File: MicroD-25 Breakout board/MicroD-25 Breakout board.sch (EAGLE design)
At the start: 1 part

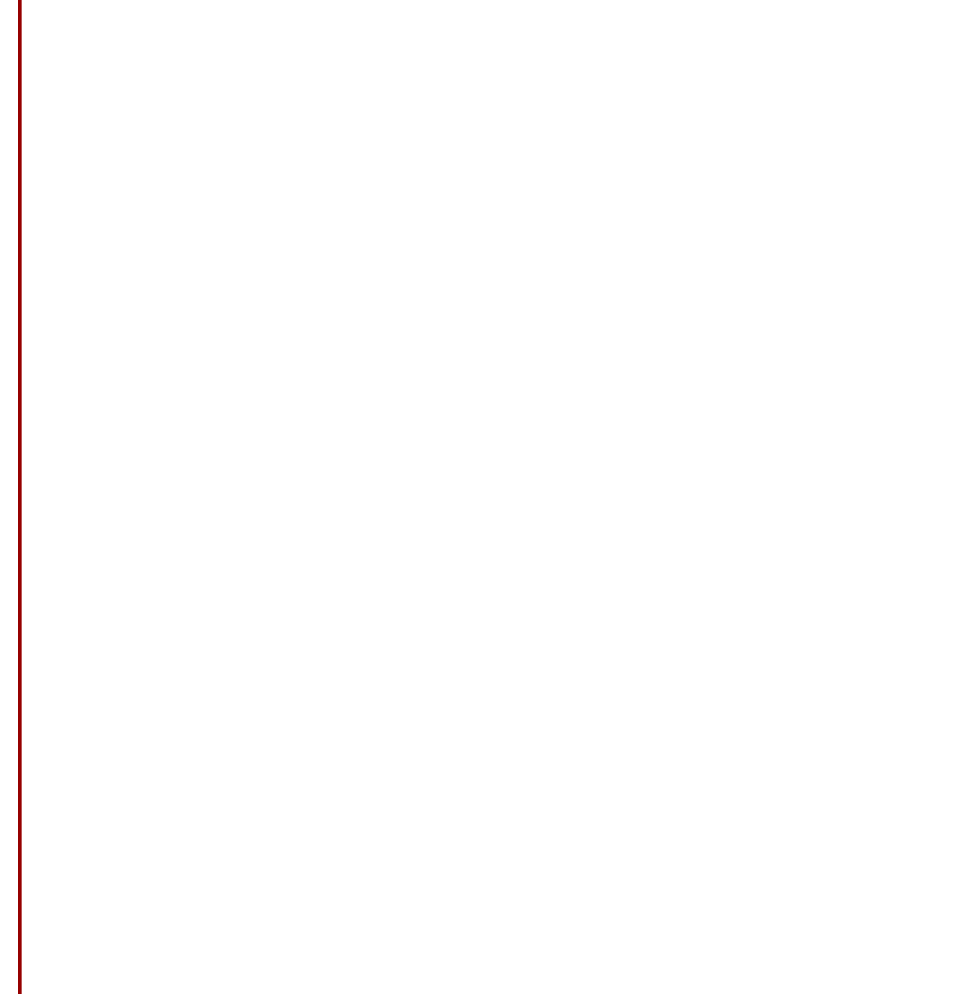
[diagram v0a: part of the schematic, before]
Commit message: Complete routing of Micro-D25 breakout board. Coordinate with MechE and send to manufacture
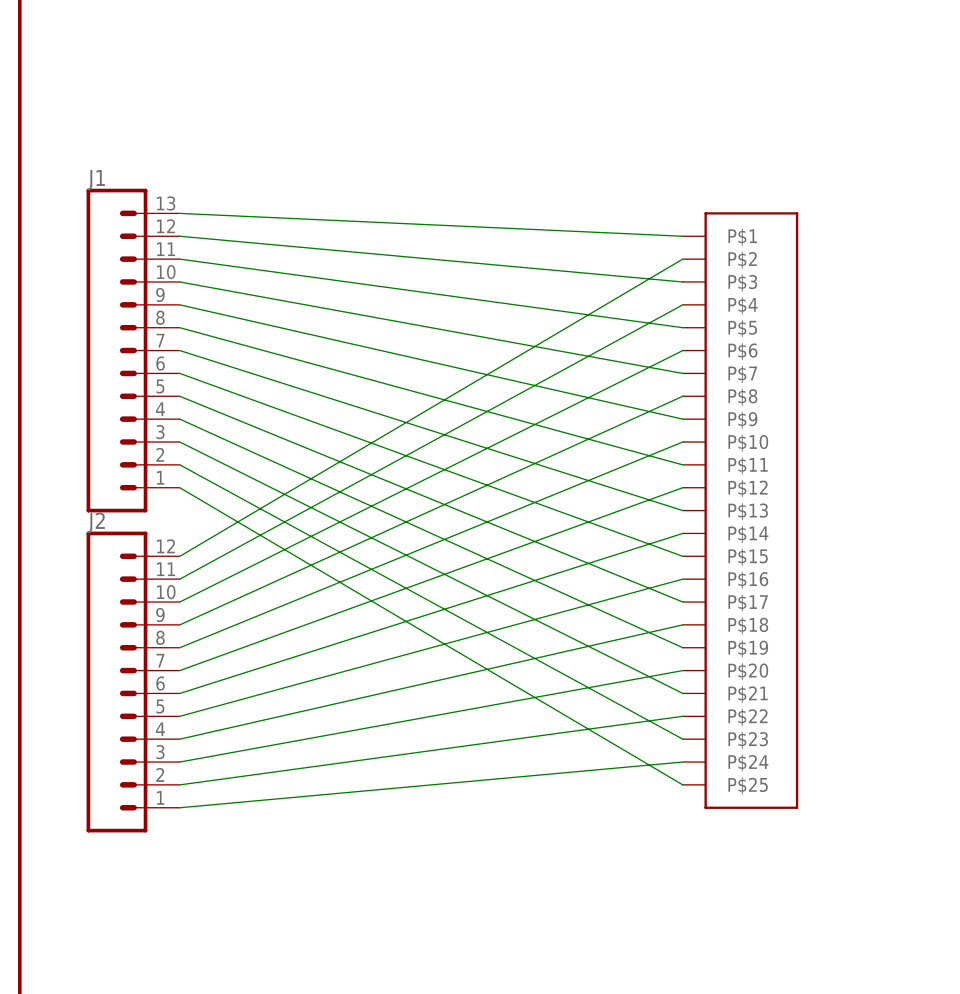
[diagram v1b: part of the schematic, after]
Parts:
- added J1: (no value), SparkFun-Connectors:CONN_13LONGPADS
- added J2: (no value), SparkFun-Connectors:CONN_12LONGPADS
- added U$1: MICROD25_FM_RCPT, Braly2:MICROD25_FM_RCPT
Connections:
- new net N$1: J1.13, U$1.P$1
- new net N$10: J1.4, U$1.P$19
- new net N$11: J1.3, U$1.P$21
- new net N$12: J1.2, U$1.P$23
- new net N$13: J1.1, U$1.P$25
- new net N$14: J2.12, U$1.P$2
- new net N$15: J2.11, U$1.P$4
- new net N$16: J2.10, U$1.P$6
- new net N$17: J2.9, U$1.P$8
- new net N$18: J2.8, U$1.P$10
- new net N$19: J2.7, U$1.P$12
- new net N$2: J1.12, U$1.P$3
- new net N$20: J2.6, U$1.P$14
- new net N$21: J2.5, U$1.P$16
- new net N$22: J2.4, U$1.P$18
- new net N$23: J2.3, U$1.P$20
- new net N$24: J2.2, U$1.P$22
- new net N$25: J2.1, U$1.P$24
- new net N$3: J1.11, U$1.P$5
- new net N$4: J1.10, U$1.P$7
- new net N$5: J1.9, U$1.P$9
- new net N$6: J1.8, U$1.P$11
- new net N$7: J1.7, U$1.P$13
- new net N$8: J1.6, U$1.P$15
- new net N$9: J1.5, U$1.P$17
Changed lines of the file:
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@@
 <parts>
 <part name="FRAME1" library="SparkFun-Aesthetics" deviceset="FRAME-LETTER" device="NO_PACKAGE"/>
+<part name="U$1" library="Braly2" deviceset="MICROD25_FM_RCPT" device=""/>
+<part name="J1" library="SparkFun-Connectors" deviceset="CONN_13" device="LONGPADS"/>
+<part name="J2" library="SparkFun-Connectors" deviceset="CONN_12" device="LONGPADS"/>
 </parts>
 <sheets>
@@
 <attribute name="DESIGNER" x="170.434" y="11.176" size="2.7432" layer="94" font="vector"/>
 </instance>
+<instance part="U$1" gate="G$1" x="76.2" y="63.5" smashed="yes"/>
+<instance part="J1" gate="G$1" x="7.62" y="76.2" smashed="yes">
+<attribute name="VALUE" x="7.62" y="56.134" size="1.778" layer="96" font="vector"/>
+<attribute name="NAME" x="7.62" y="94.488" size="1.778" layer="95" font="vector"/>
+</instance>
+<instance part="J2" gate="G$1" x="7.62" y="40.64" smashed="yes">
+<attribute name="VALUE" x="7.62" y="20.574" size="1.778" layer="96" font="vector"/>
+<attribute name="NAME" x="7.62" y="56.388" size="1.778" layer="95" font="vector"/>
+</instance>
 </instances>
 <busses>
 </busses>
 <nets>
+<net name="N$14" class="0">
+<segment>
+<pinref part="U$1" gate="G$1" pin="P$2"/>
+<pinref part="J2" gate="G$1" pin="12"/>
+<wire x1="73.66" y1="86.36" x2="17.78" y2="53.34" width="0.1524" layer="91"/>
+</segment>
+</net>
+<net name="N$15" class="0">
+<segment>
+<pinref part="U$1" gate="G$1" pin="P$4"/>
+<pinref part="J2" gate="G$1" pin="11"/>
+<wire x1="73.66" y1="81.28" x2="17.78" y2="50.8" width="0.1524" layer="91"/>
+</segment>
+</net>
+<net name="N$16" class="0">
+<segment>
+<pinref part="U$1" gate="G$1" pin="P$6"/>
+<pinref part="J2" gate="G$1" pin="10"/>
+<wire x1="73.66" y1="76.2" x2="17.78" y2="48.26" width="0.1524" layer="91"/>
+</segment>
+</net>
+<net name="N$17" class="0">
+<segment>
+<pinref part="U$1" gate="G$1" pin="P$8"/>
+<pinref part="J2" gate="G$1" pin="9"/>
+<wire x1="73.66" y1="71.12" x2="17.78" y2="45.72" width="0.1524" layer="91"/>
+</segment>
+</net>
+<net name="N$18" class="0">
+<segment>
+<pinref part="U$1" gate="G$1" pin="P$10"/>
+<pinref part="J2" gate="G$1" pin="8"/>
+<wire x1="73.66" y1="66.04" x2="17.78" y2="43.18" width="0.1524" layer="91"/>
+</segment>
+</net>
+<net name="N$19" class="0">
+<segment>
+<pinref part="U$1" gate="G$1" pin="P$12"/>
+<pinref part="J2" gate="G$1" pin="7"/>
+<wire x1="73.66" y1="60.96" x2="17.78" y2="40.64" width="0.1524" layer="91"/>
+</segment>
+</net>
+<net name="N$20" class="0">
+<segment>
+<pinref part="U$1" gate="G$1" pin="P$14"/>
+<pinref part="J2" gate="G$1" pin="6"/>
+<wire x1="73.66" y1="55.88" x2="17.78" y2="38.1" width="0.1524" layer="91"/>
+</segment>
+</net>
+<net name="N$21" class="0">
+<segment>
+<pinref part="U$1" gate="G$1" pin="P$16"/>
+<pinref part="J2" gate="G$1" pin="5"/>
+<wire x1="73.66" y1="50.8" x2="17.78" y2="35.56" width="0.1524" layer="91"/>
+</segment>
+</net>
+<net name="N$22" class="0">
+<segment>
+<pinref part="U$1" gate="G$1" pin="P$18"/>
+<pinref part="J2" gate="G$1" pin="4"/>
+<wire x1="73.66" y1="45.72" x2="17.78" y2="33.02" width="0.1524" layer="91"/>
+</segment>
+</net>
+<net name="N$23" class="0">
+<segment>
+<pinref part="U$1" gate="G$1" pin="P$20"/>
+<pinref part="J2" gate="G$1" pin="3"/>
+<wire x1="73.66" y1="40.64" x2="17.78" y2="30.48" width="0.1524" layer="91"/>
+</segment>
+</net>
+<net name="N$24" class="0">
+<segment>
+<pinref part="U$1" gate="G$1" pin="P$22"/>
+<pinref part="J2" gate="G$1" pin="2"/>
+<wire x1="73.66" y1="35.56" x2="17.78" y2="27.94" width="0.1524" layer="91"/>
+</segment>
+</net>
+<net name="N$25" class="0">
+<segment>
+<pinref part="U$1" gate="G$1" pin="P$24"/>
+<pinref part="J2" gate="G$1" pin="1"/>
+<wire x1="73.66" y1="30.48" x2="17.78" y2="25.4" width="0.1524" layer="91"/>
+</segment>
+</net>
+<net name="N$1" class="0">
+<segment>
+<pinref part="U$1" gate="G$1" pin="P$1"/>
+<pinref part="J1" gate="G$1" pin="13"/>
+<wire x1="73.66" y1="88.9" x2="17.78" y2="91.44" width="0.1524" layer="91"/>
+</segment>
+</net>
+<net name="N$2" class="0">
+<segment>
+<pinref part="U$1" gate="G$1" pin="P$3"/>
+<pinref part="J1" gate="G$1" pin="12"/>
+<wire x1="73.66" y1="83.82" x2="17.78" y2="88.9" width="0.1524" layer="91"/>
+</segment>
+</net>
+<net name="N$3" class="0">
+<segment>
+<pinref part="U$1" gate="G$1" pin="P$5"/>
+<pinref part="J1" gate="G$1" pin="11"/>
+<wire x1="73.66" y1="78.74" x2="17.78" y2="86.36" width="0.1524" layer="91"/>
+</segment>
+</net>
+<net name="N$4" class="0">
+<segment>
+<pinref part="U$1" gate="G$1" pin="P$7"/>
+<pinref part="J1" gate="G$1" pin="10"/>
+<wire x1="73.66" y1="73.66" x2="17.78" y2="83.82" width="0.1524" layer="91"/>
+</segment>
+</net>
+<net name="N$5" class="0">
+<segment>
+<pinref part="U$1" gate="G$1" pin="P$9"/>
+<pinref part="J1" gate="G$1" pin="9"/>
+<wire x1="73.66" y1="68.58" x2="17.78" y2="81.28" width="0.1524" layer="91"/>
+</segment>
+</net>
+<net name="N$6" class="0">
+<segment>
+<pinref part="U$1" gate="G$1" pin="P$11"/>
+<pinref part="J1" gate="G$1" pin="8"/>
+<wire x1="73.66" y1="63.5" x2="17.78" y2="78.74" width="0.1524" layer="91"/>
+</segment>
+</net>
+<net name="N$7" class="0">
+<segment>
+<pinref part="U$1" gate="G$1" pin="P$13"/>
+<pinref part="J1" gate="G$1" pin="7"/>
+<wire x1="73.66" y1="58.42" x2="17.78" y2="76.2" width="0.1524" layer="91"/>
+</segment>
+</net>
+<net name="N$8" class="0">
+<segment>
+<pinref part="U$1" gate="G$1" pin="P$15"/>
+<pinref part="J1" gate="G$1" pin="6"/>
+<wire x1="73.66" y1="53.34" x2="17.78" y2="73.66" width="0.1524" layer="91"/>
+</segment>
+</net>
+<net name="N$9" class="0">
+<segment>
+<pinref part="U$1" gate="G$1" pin="P$17"/>
+<pinref part="J1" gate="G$1" pin="5"/>
+<wire x1="73.66" y1="48.26" x2="17.78" y2="71.12" width="0.1524" layer="91"/>
+</segment>
+</net>
+<net name="N$10" class="0">
+<segment>
+<pinref part="U$1" gate="G$1" pin="P$19"/>
+<pinref part="J1" gate="G$1" pin="4"/>
+<wire x1="73.66" y1="43.18" x2="17.78" y2="68.58" width="0.1524" layer="91"/>
+</segment>
+</net>
+<net name="N$11" class="0">
+<segment>
+<pinref part="U$1" gate="G$1" pin="P$21"/>
+<pinref part="J1" gate="G$1" pin="3"/>
+<wire x1="73.66" y1="38.1" x2="17.78" y2="66.04" width="0.1524" layer="91"/>
+</segment>
+</net>
+<net name="N$12" class="0">
+<segment>
+<pinref part="U$1" gate="G$1" pin="P$23"/>
+<pinref part="J1" gate="G$1" pin="2"/>
+<wire x1="73.66" y1="33.02" x2="17.78" y2="63.5" width="0.1524" layer="91"/>
+</segment>
+</net>
+<net name="N$13" class="0">
+<segment>
+<pinref part="U$1" gate="G$1" pin="P$25"/>
+<pinref part="J1" gate="G$1" pin="1"/>
+<wire x1="73.66" y1="27.94" x2="17.78" y2="60.96" width="0.1524" layer="91"/>
+</segment>
+</net>
 </nets>
 </sheet>
